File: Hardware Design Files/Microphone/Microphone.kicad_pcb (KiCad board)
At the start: 2 copper layers, 43.3 x 21.6 mm, 22 parts, among them J1 TP1, J2 TP2, J3 TP3, J4 TP4, J5 TP5, J6 VDD GND MIC_OUT, U1 MAX4466

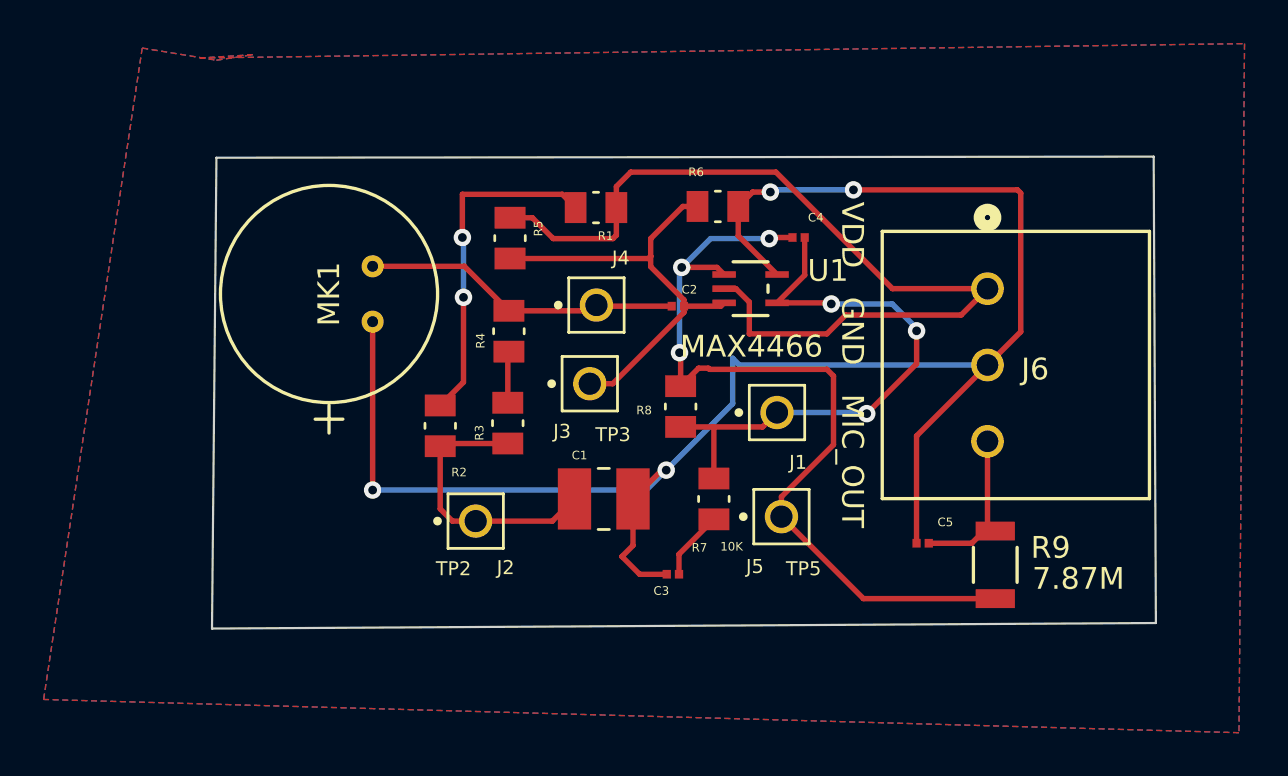
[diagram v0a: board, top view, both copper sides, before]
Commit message: Adjusted Edge cuts
Adjusted Edge cuts and excluded DRC
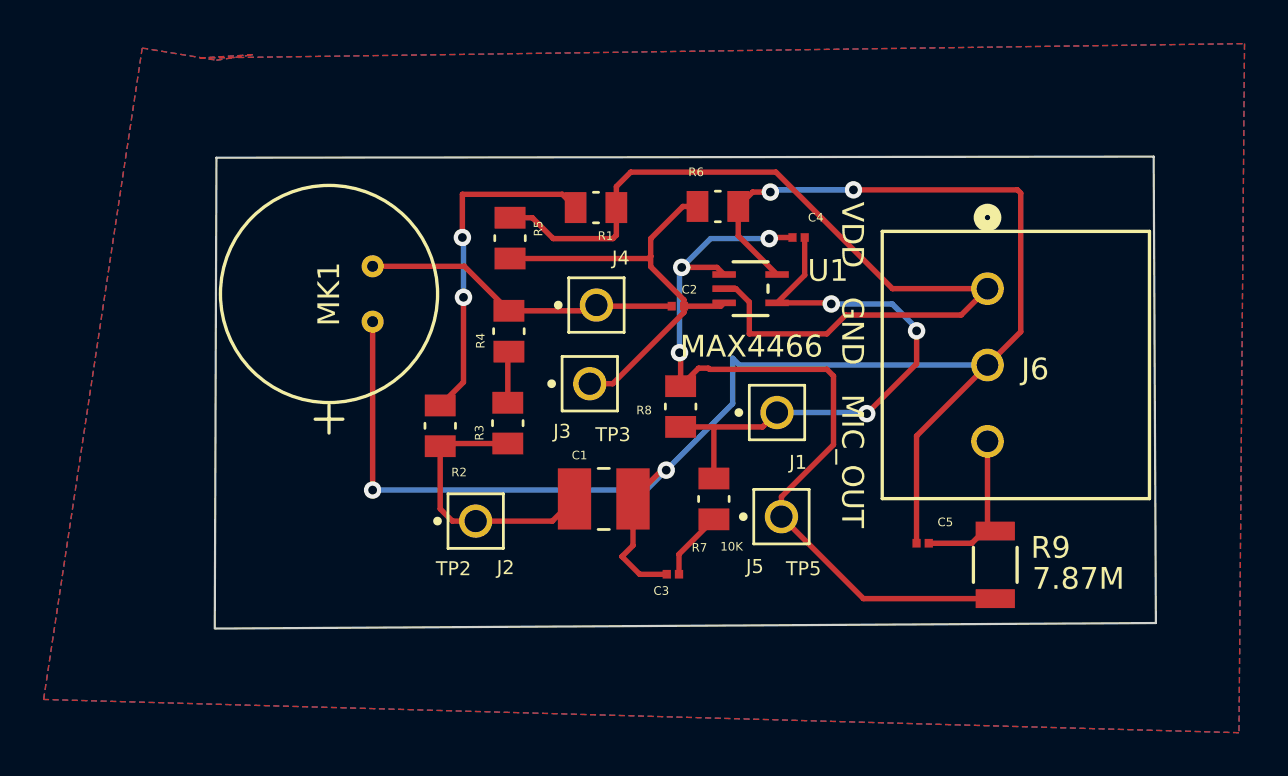
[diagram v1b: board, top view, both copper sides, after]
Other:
- board size 43.3 x 21.6 mm -> 43.2 x 21.6 mm
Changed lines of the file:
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@@
   (gr_line (start 39.7764 152.4) (end 159.512 152.3492)
     (stroke (width 0.15) (type default)) (layer "Cmts.User"))
-  (gr_line (start 172.7454 99.8982) (end 129.4638 100.1522)
+  (gr_line (start 172.7454 99.8982) (end 129.6416 100.1522)
     (stroke (width 0.1) (type default)) (layer "Edge.Cuts"))
   (gr_line (start 129.667 78.5622) (end 172.6438 78.5114)
@@
   (gr_line (start 172.6438 78.5114) (end 172.7454 99.8982)
     (stroke (width 0.1) (type default)) (layer "Edge.Cuts"))
-  (gr_line (start 129.4638 100.1522) (end 129.667 78.5622)
+  (gr_line (start 129.5908 100.1522) (end 129.667 78.5622)
     (stroke (width 0.1) (type default)) (layer "Edge.Cuts"))
   (gr_text "***************			Revision Table			***************\n				\nDate		Author	Description\n12/29/2023	EN		Initial Creation" (at 40.2844 161.7472) (layer "Cmts.User")

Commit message: Updated footprint library
Made footprint library the appropriate format such that pulling files does not require as much work for a clean DRC
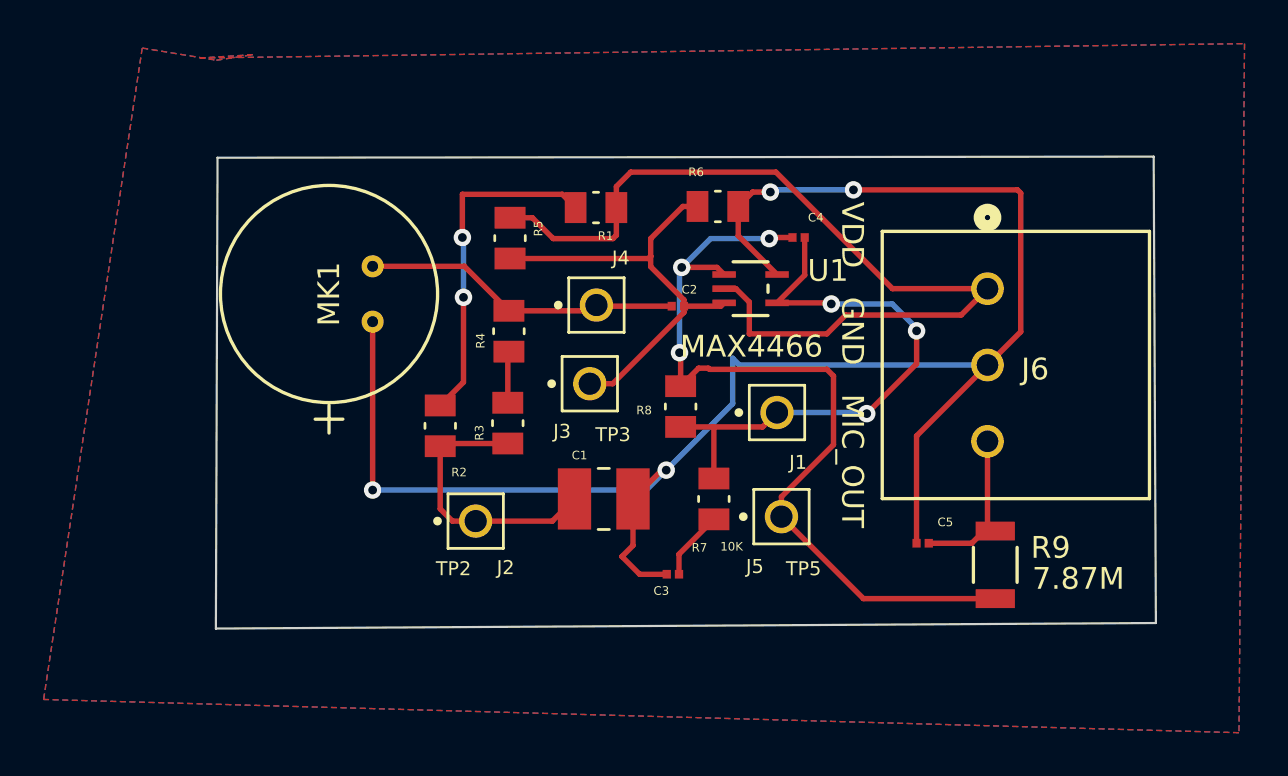
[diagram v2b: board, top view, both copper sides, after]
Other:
- board size 43.2 x 21.6 mm -> 43.1 x 21.6 mm
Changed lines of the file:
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@@
   (gr_line (start 172.7454 99.8982) (end 129.6416 100.1522)
     (stroke (width 0.1) (type default)) (layer "Edge.Cuts"))
-  (gr_line (start 129.667 78.5622) (end 172.6438 78.5114)
+  (gr_line (start 129.7178 78.5622) (end 172.6438 78.5114)
     (stroke (width 0.1) (type default)) (layer "Edge.Cuts"))
   (gr_line (start 172.6438 78.5114) (end 172.7454 99.8982)
     (stroke (width 0.1) (type default)) (layer "Edge.Cuts"))
-  (gr_line (start 129.5908 100.1522) (end 129.667 78.5622)
+  (gr_line (start 129.6416 100.1522) (end 129.7178 78.5622)
     (stroke (width 0.1) (type default)) (layer "Edge.Cuts"))
   (gr_text "***************			Revision Table			***************\n				\nDate		Author	Description\n12/29/2023	EN		Initial Creation" (at 40.2844 161.7472) (layer "Cmts.User")

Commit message: Returned PCB Files
Previous commit accidentally ommitted footprint files. This change rectifies this
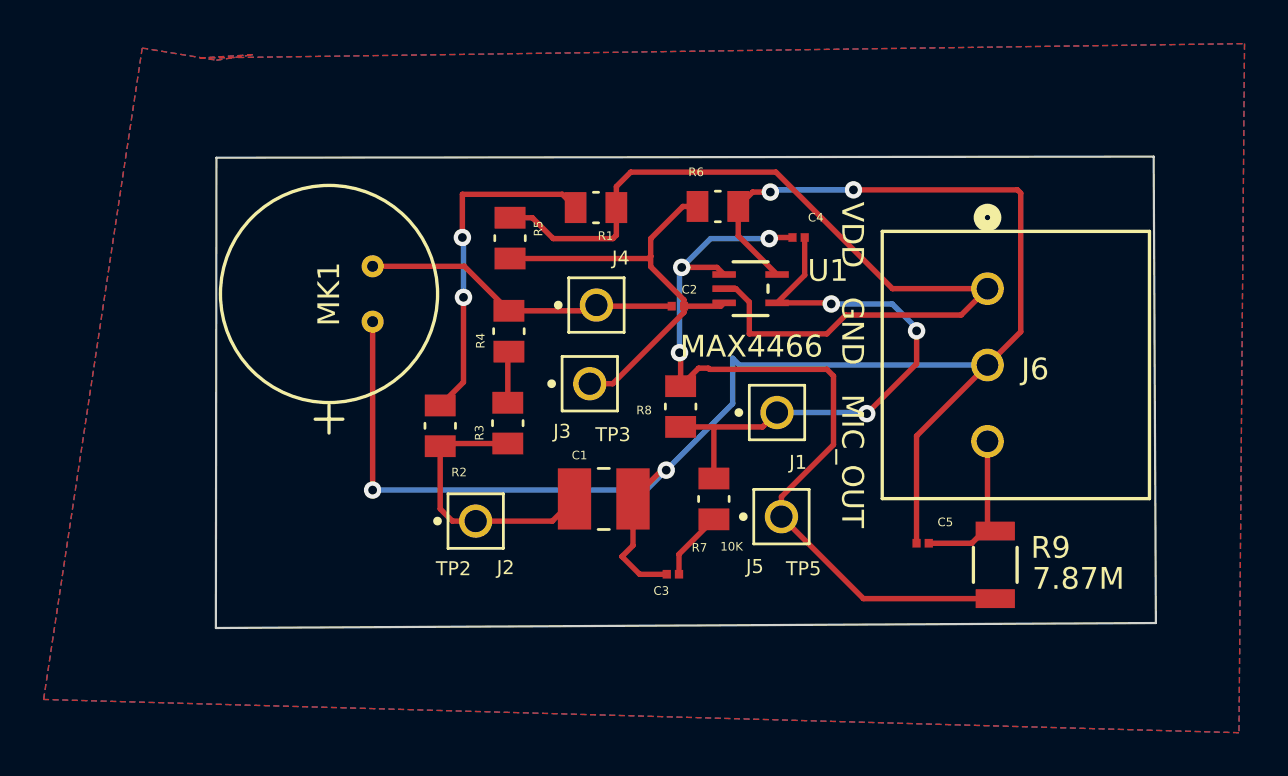
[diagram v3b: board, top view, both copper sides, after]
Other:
- outline, holes or cut-outs redrawn
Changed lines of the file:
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@@
   (gr_line (start 39.7764 152.4) (end 159.512 152.3492)
     (stroke (width 0.15) (type default)) (layer "Cmts.User"))
-  (gr_line (start 172.7454 99.8982) (end 129.6416 100.1522)
+  (gr_line (start 172.7454 99.8982) (end 129.6416 100.1268)
     (stroke (width 0.1) (type default)) (layer "Edge.Cuts"))
-  (gr_line (start 129.7178 78.5622) (end 172.6438 78.5114)
+  (gr_line (start 129.667 78.5622) (end 172.6438 78.5114)
     (stroke (width 0.1) (type default)) (layer "Edge.Cuts"))
   (gr_line (start 172.6438 78.5114) (end 172.7454 99.8982)
     (stroke (width 0.1) (type default)) (layer "Edge.Cuts"))
-  (gr_line (start 129.6416 100.1522) (end 129.7178 78.5622)
+  (gr_line (start 129.6416 100.1268) (end 129.667 78.5622)
     (stroke (width 0.1) (type default)) (layer "Edge.Cuts"))
   (gr_text "***************			Revision Table			***************\n				\nDate		Author	Description\n12/29/2023	EN		Initial Creation" (at 40.2844 161.7472) (layer "Cmts.User")

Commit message: changed R1
changed from 10k to 70k such that chip select current ~5ua
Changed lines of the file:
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@@
         (effects (font (size 0.393701 0.393701) (thickness 0.098425)))
     )
-    (fp_text value "1.8M" (at 1.1382 -1.4732) (layer "F.Fab")
-        (effects (font (size 0.393701 0.393701) (thickness 0.15)))
+    (fp_text value "1.8M" (at 1.1382 -1.4732) (layer "F.SilkS")
+        (effects (font (size 0.393701 0.393701) (thickness 0.098425)))
     )
     (fp_line (start -0.12 -0.7) (end 0.12 -0.7)
@@
         (effects (font (size 0.393701 0.393701) (thickness 0.15)))
     )
-    (fp_text value "1k" (at 1.31 1.3) (layer "F.Fab")
-        (effects (font (size 0.393701 0.393701) (thickness 0.15)))
+    (fp_text value "1k" (at 1.31 1.3) (layer "F.SilkS")
+        (effects (font (size 0.393701 0.393701) (thickness 0.098425)))
     )
     (fp_line (start -0.12 -0.7) (end 0.12 -0.7)
@@
         (effects (font (size 0.393701 0.393701) (thickness 0.098425)))
     )
-    (fp_text value "100" (at 2.1844 0.8636 -180) (layer "F.Fab")
-        (effects (font (size 0.393701 0.393701) (thickness 0.15)))
+    (fp_text value "100" (at 2.1844 0.8636 180) (layer "F.SilkS")
+        (effects (font (size 0.393701 0.393701) (thickness 0.098425)))
     )
     (fp_line (start -0.12 -0.7) (end 0.12 -0.7)
@@
         (effects (font (size 0.393701 0.393701) (thickness 0.15)))
     )
-    (fp_text value "100" (at 1.31 1.3 90) (layer "F.Fab")
-        (effects (font (size 0.393701 0.393701) (thickness 0.15)))
+    (fp_text value "100" (at 1.31 1.3 90) (layer "F.SilkS")
+        (effects (font (size 0.393701 0.393701) (thickness 0.098425)))
     )
     (fp_line (start -0.12 -0.7) (end 0.12 -0.7)
@@
         (effects (font (size 0.393701 0.393701) (thickness 0.15)))
     )
-    (fp_text value "499k" (at 0.5382 -1.778 180) (layer "F.Fab")
-        (effects (font (size 0.393701 0.393701) (thickness 0.15)))
+    (fp_text value "499k" (at 0.5382 -1.778 180) (layer "F.SilkS")
+        (effects (font (size 0.393701 0.393701) (thickness 0.098425)))
     )
     (fp_line (start -0.12 -0.7) (end 0.12 -0.7)
@@
     (property "ki_keywords" "R res resistor")
     (attr smd)
-    (fp_text reference "R3" (at -0.44 -1.3 90) (layer "F.SilkS")
+    (fp_text reference "R3" (at -0.0968 -1.4478 180) (layer "F.SilkS")
         (effects (font (size 0.393701 0.393701) (thickness 0.15)))
     )
-    (fp_text value "1k" (at 1.31 1.3 90) (layer "F.Fab")
-        (effects (font (size 0.393701 0.393701) (thickness 0.15)))
+    (fp_text value "1k" (at 0.9192 -1.3462 180) (layer "F.SilkS")
+        (effects (font (size 0.393701 0.393701) (thickness 0.098425)))
     )
     (fp_line (start -0.12 -0.7) (end 0.12 -0.7)
@@
         (effects (font (size 0.393701 0.393701) (thickness 0.15)))
     )
-    (fp_text value "12n" (at -0.8874 -0.8636) (layer "F.Fab")
-        (effects (font (size 0.393701 0.393701) (thickness 0.15)))
+    (fp_text value "12n" (at -0.8874 -0.8636) (layer "F.SilkS")
+        (effects (font (size 0.393701 0.393701) (thickness 0.098425)))
     )
     (fp_line (start -0.718 -0.448) (end 0.718 -0.448)
@@
         (effects (font (size 0.393701 0.393701) (thickness 0.15)))
     )
-    (fp_text value "1u" (at 2.28 0.76) (layer "F.Fab")
-        (effects (font (size 0.393701 0.393701) (thickness 0.15)))
+    (fp_text value "1u" (at -0.8382 -0.7366) (layer "F.SilkS")
+        (effects (font (size 0.393701 0.393701) (thickness 0.098425)))
     )
     (fp_line (start -0.718 -0.448) (end 0.718 -0.448)
@@
         (effects (font (size 0.393701 0.393701) (thickness 0.15)))
     )
-    (fp_text value "1p" (at 0.535 1.016) (layer "F.Fab")
-        (effects (font (size 0.393701 0.393701) (thickness 0.15)))
+    (fp_text value "1p" (at 0.535 1.016) (layer "F.SilkS")
+        (effects (font (size 0.393701 0.393701) (thickness 0.098425)))
     )
     (fp_line (start -0.718 -0.448) (end 0.718 -0.448)
@@
         (effects (font (size 0.64 0.64) (thickness 0.15)))
     )
-    (fp_text value "TP4" (at -0.8128 -2.1336) (layer "F.Fab")
+    (fp_text value "TP4" (at -0.8128 -2.1336) (layer "F.SilkS")
         (effects (font (size 0.64 0.64) (thickness 0.15)))
     )
@@
     (property "ki_keywords" "cap capacitor")
     (attr smd)
-    (fp_text reference "C1" (at -1.11 -2) (layer "F.SilkS")
+    (fp_text reference "C1" (at -1.072 1.9558) (layer "F.SilkS")
         (effects (font (size 0.393701 0.393701) (thickness 0.15)))
     )
-    (fp_text value "330u" (at 0.89 2) (layer "F.Fab")
-        (effects (font (size 0.393701 0.393701) (thickness 0.15)))
+    (fp_text value "330u" (at 0.89 2) (layer "F.SilkS")
+        (effects (font (size 0.393701 0.393701) (thickness 0.098425)))
     )
     (fp_line (start -0.26 -1.4) (end 0.26 -1.4)
@@
         (effects (font (size 0.393701 0.393701) (thickness 0.098425)))
     )
-    (fp_text value "100p" (at 0.8366 0.9652) (layer "F.Fab")
-        (effects (font (size 0.393701 0.393701) (thickness 0.15)))
+    (fp_text value "100p" (at 0.8366 0.9652) (layer "F.SilkS")
+        (effects (font (size 0.393701 0.393701) (thickness 0.098425)))
     )
     (fp_line (start -0.718 -0.448) (end 0.718 -0.448)
@@
         (effects (font (size 0.393701 0.393701) (thickness 0.15)))
     )
-    (fp_text value "1M" (at 1.31 1.3 90) (layer "F.Fab")
-        (effects (font (size 0.393701 0.393701) (thickness 0.15)))
+    (fp_text value "1M" (at 1.31 1.3 90) (layer "F.SilkS")
+        (effects (font (size 0.393701 0.393701) (thickness 0.098425)))
     )
     (fp_line (start -0.12 -0.7) (end 0.12 -0.7)
@@
         (effects (font (size 0.64 0.64) (thickness 0.15)))
     )
-    (fp_text value "TP1" (at -0.8128 2.3368) (layer "F.Fab")
-        (effects (font (size 0.64 0.64) (thickness 0.15)))
-    )
+    (fp_text value "TP1" (at -0.8128 2.3368) (layer "F.SilkS")
+        (effects (font (size 0.64 0.64) (thickness 0.15)))
+    )
